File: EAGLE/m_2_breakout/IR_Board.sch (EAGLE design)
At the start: 38 parts, among them X1 C-GRID-14-70543, X10 C-GRID-02-70553, X11 C-GRID-02-70553, X12 C-GRID-02-70553, X2 C-GRID-14-70543, X3 C-GRID-02-70553, X4 C-GRID-02-70553, X5 C-GRID-02-70553, X6 C-GRID-02-70553, X7 C-GRID-02-70553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

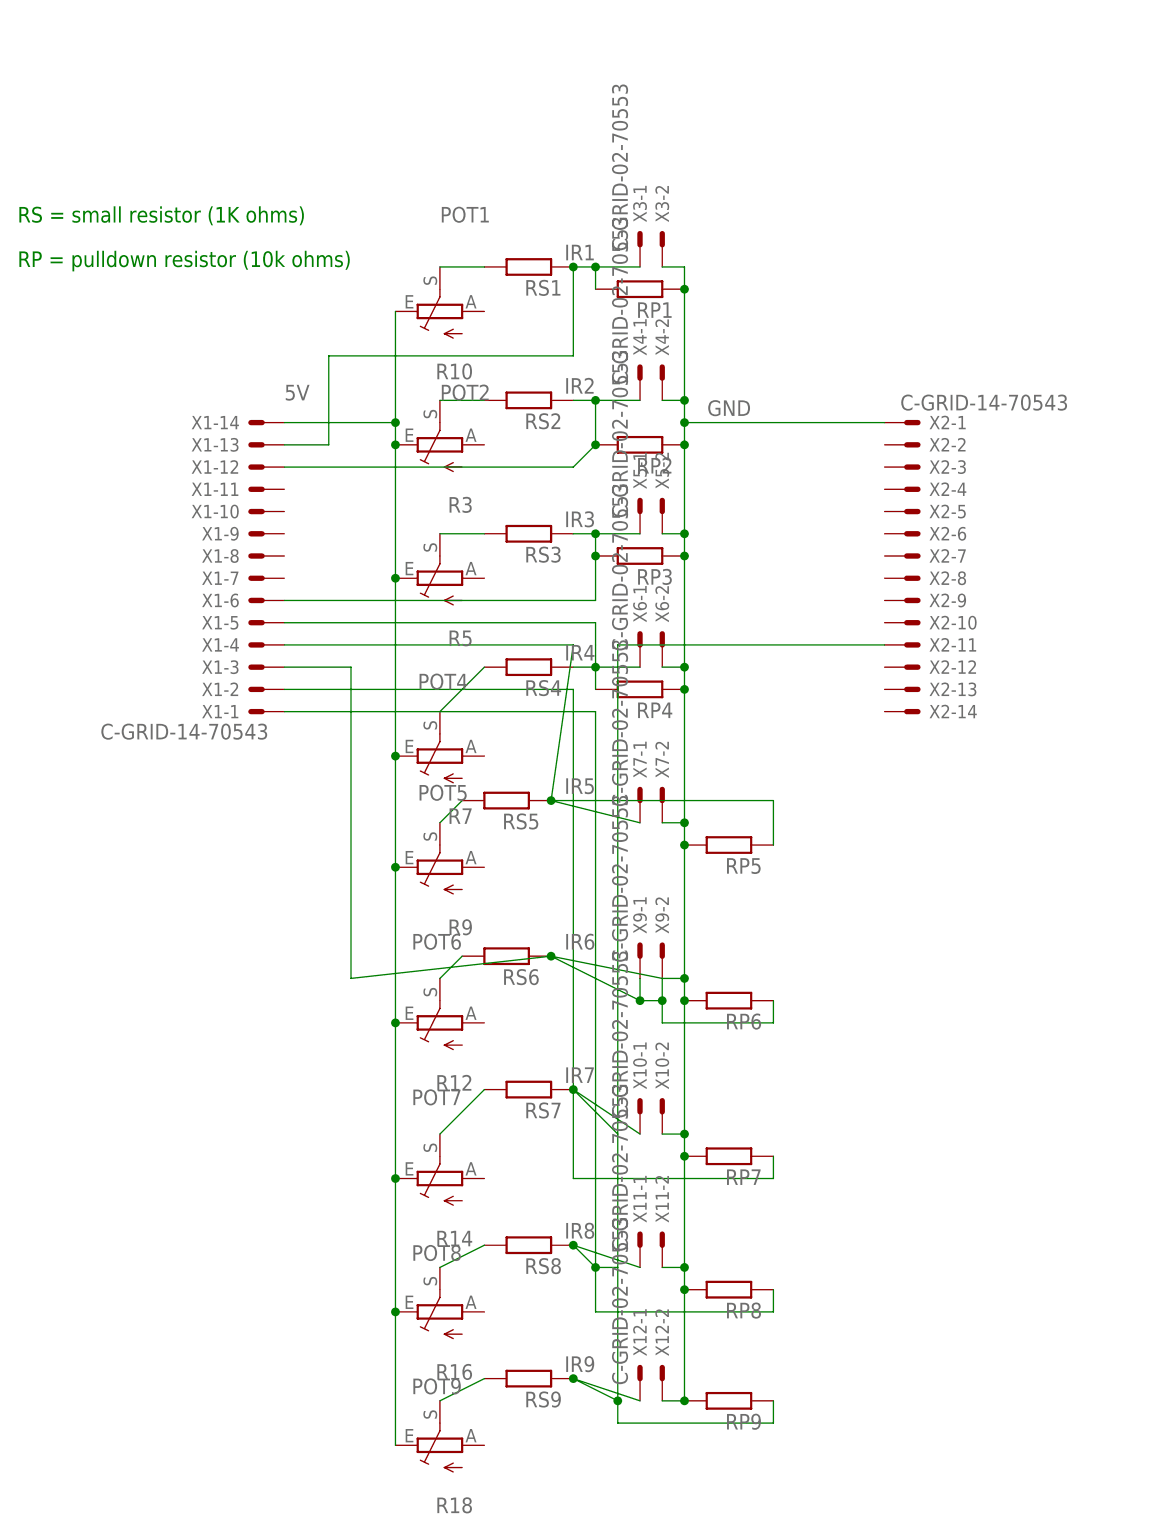
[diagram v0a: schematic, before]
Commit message: Added updated IR board schematic with correct pots
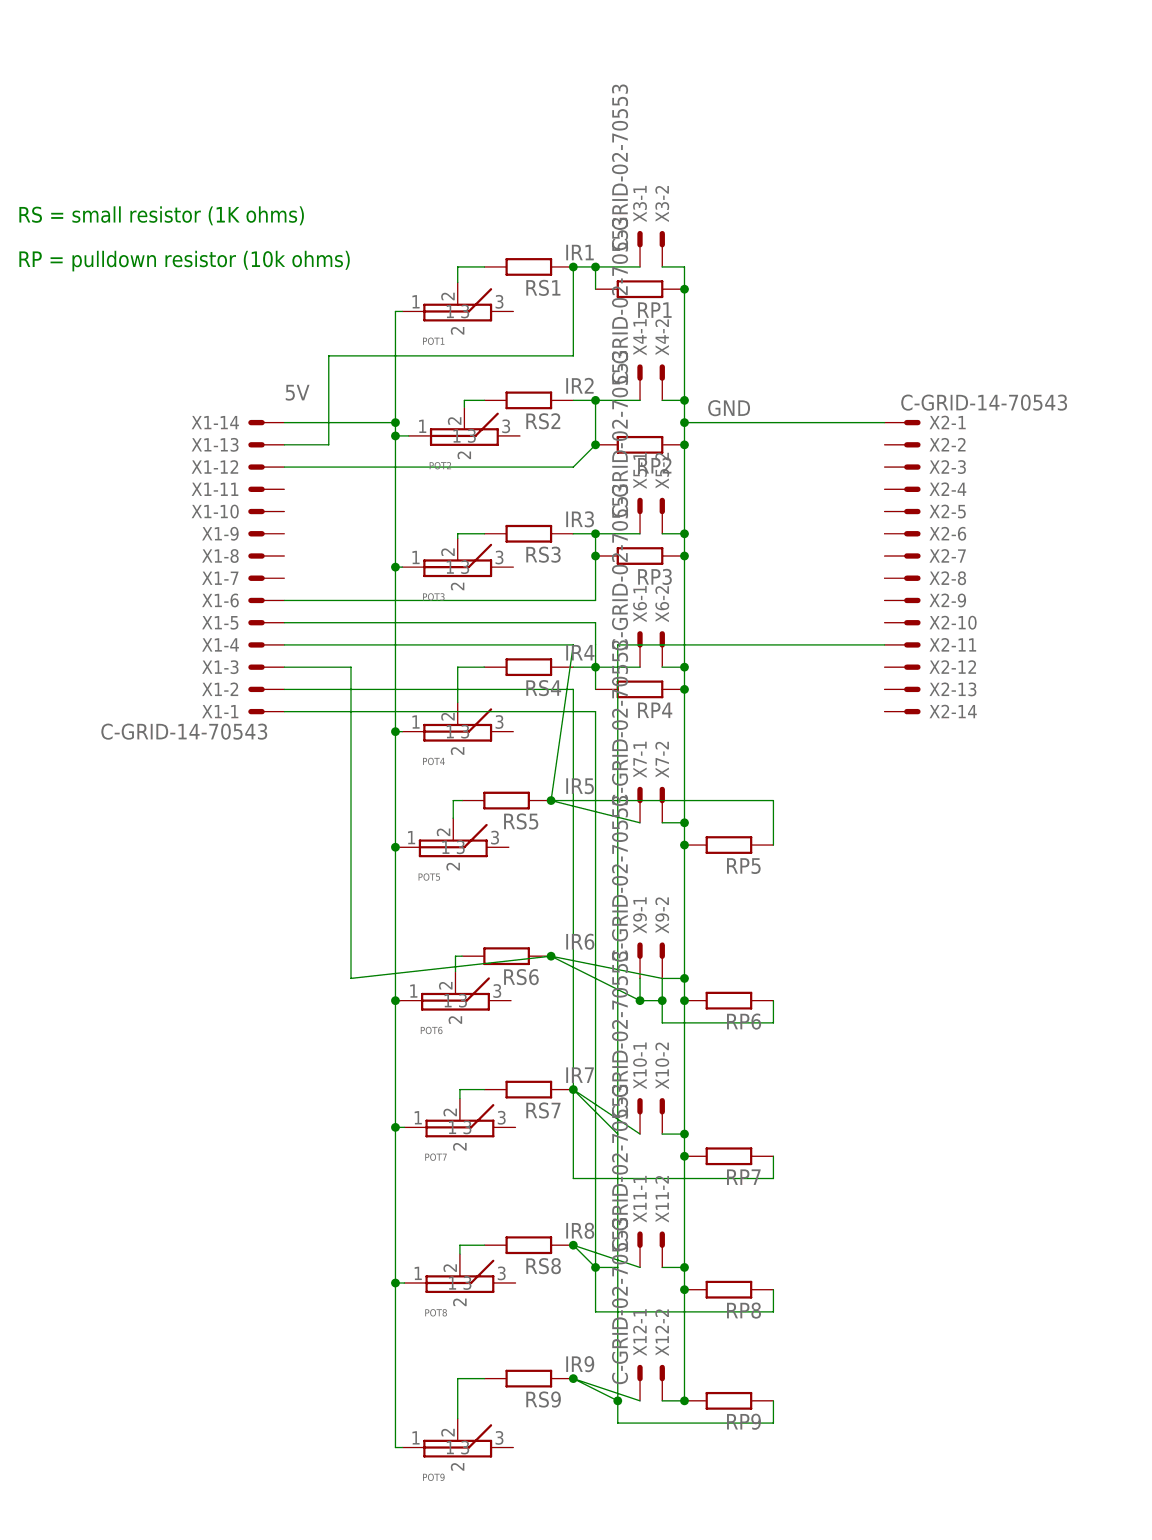
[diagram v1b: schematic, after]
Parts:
- removed R10, R12, R14, R16, R18, R3, R5, R7, R9: (no value), pot:TRIM_EU-B25P
- added POT1, POT2, POT3, POT4, POT5, POT6, POT7, POT8, POT9: POTENTIOMETER_1, ben_kramer:POTENTIOMETER_1
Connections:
- removed net POT1: R10.S, RS1.2
- removed net POT2: R3.S, RS2.2
- removed net POT3: R5.S, RS3.2
- removed net POT4: R7.S, RS4.2
- removed net POT5: R9.S, RS5.2
- removed net POT6: R12.S, RS6.2
- removed net POT7: R14.S, RS7.2
- removed net POT8: R16.S, RS8.2
- removed net POT9: R18.S, RS9.2
- new net N$1: POT1.2, RS1.2
- new net N$2: POT3.2, RS3.2
- new net N$3: POT2.2, RS2.2
- new net N$4: POT5.2, RS5.2
- new net N$5: POT6.2, RS6.2
- new net N$6: POT7.2, RS7.2
- new net N$7: POT9.2, RS9.2
- new net N$8: POT8.2, RS8.2
- new net N$9: POT4.2, RS4.2
- net 5V: now also POT1.1, POT2.1, POT3.1, POT4.1, POT5.1, POT6.1, POT7.1, POT8.1, POT9.1; no longer R10.E, R12.E, R14.E, R16.E, R18.E, R3.E, R5.E, R7.E, R9.E
